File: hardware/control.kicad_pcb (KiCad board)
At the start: 2 copper layers, 49 parts, among them P1 POWER, P2 POWER, P3 DATA, P4 DATA, P5 ISP, P6 CONN_1, P7 CONN_1, P8 DISPLAY, P9 I2C, Q1 NX2301P, Q10 NX2301P, Q11 NX2301P, Q12 NX2301P, Q13 NX2301P, Q14 NX2301P, Q15 NX2301P, Q16 NX2301P, Q2 NX2301P, Q3 NX2301P, Q4 NX2301P, Q5 NX2301P, Q6 NX2301P, Q7 NX2301P, Q8 NX2301P, Q9 NX2301P, SW1 RESET, U1 AP1509, U2 ATMEGA328P-P, U3 74HC138, U4 74HC138, U5 TLC5940, X1 16MHz

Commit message: Final hardware tweaks.
Signed-off-by: Paul Brook <paul@nowt.org>
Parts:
- Q1, Q10, Q11, Q12, Q13, Q14, Q15, Q16, Q2, Q3, Q4, Q5, Q6, Q7, Q8, Q9: footprint SOT23GDS -> SOT23GDS_NP

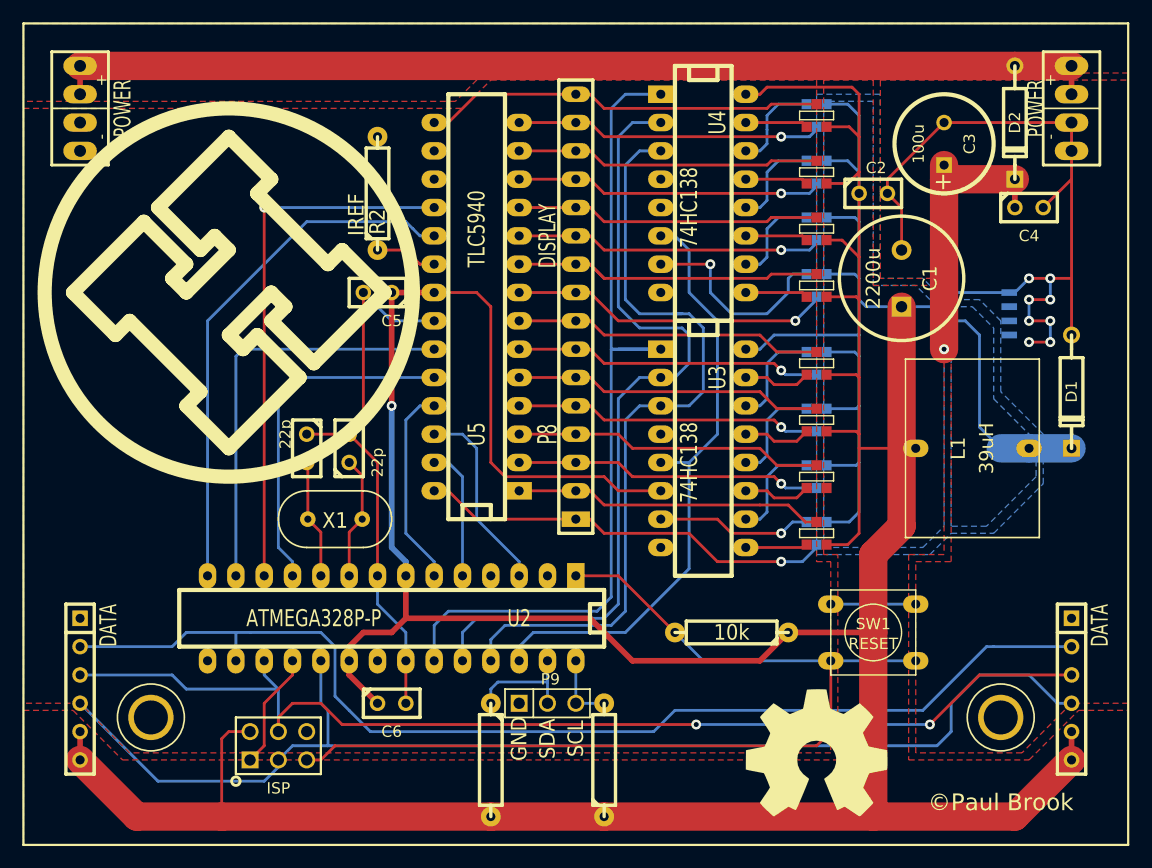
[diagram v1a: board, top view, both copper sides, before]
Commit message: PCB fixes.
Tweak power plane. Move mounting holes. Fix soldermask on power
connector.

Signed-off-by: Paul Brook <paul@nowt.org>
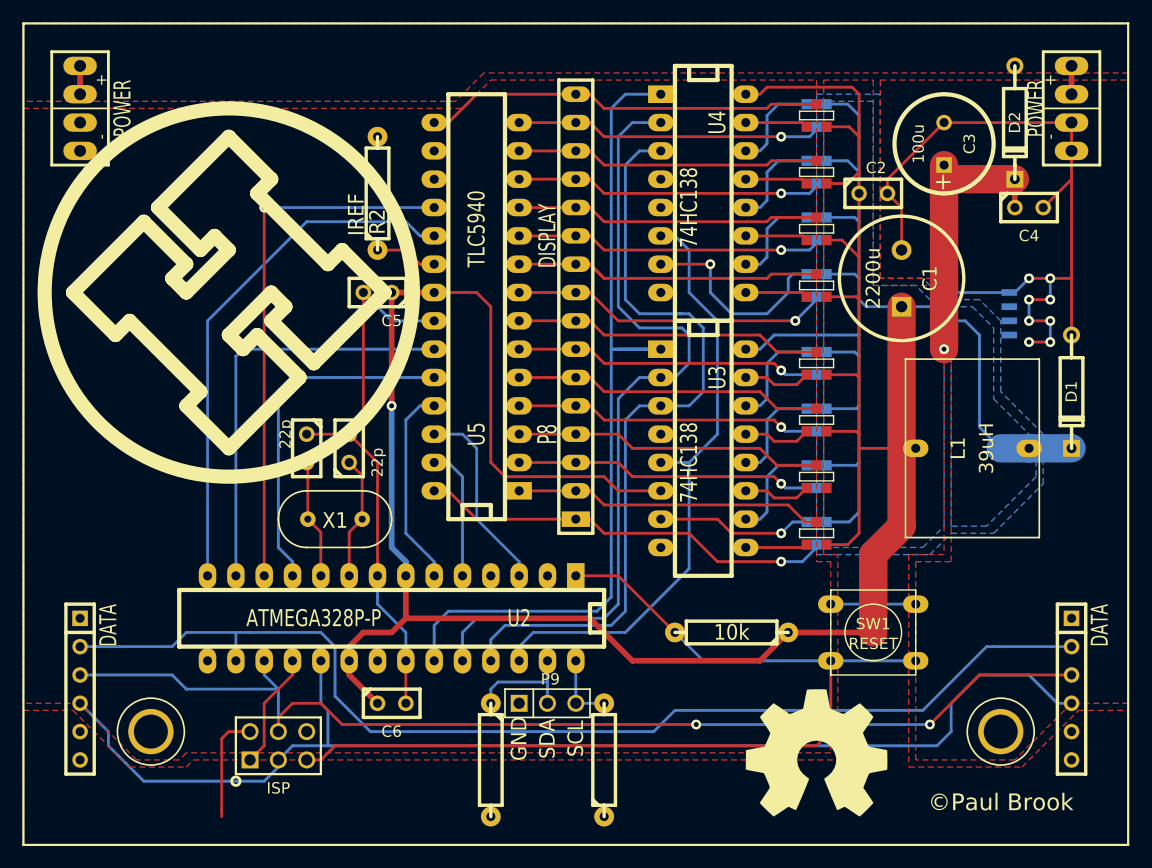
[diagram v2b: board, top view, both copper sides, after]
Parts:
- moved P6 1.27 mm to (139.7, 115.6)
- moved P7 1.27 mm to (63.5, 115.6)
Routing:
- net /5v: track 438.6 -> 323.9 mm
- net /raw: track 94.0 -> 5.08 mm
- net /SCK: track 106.5 -> 107.3 mm
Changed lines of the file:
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@@
-(kicad_pcb (version 3) (host pcbnew "(2013-dec-23)-stable")
+(kicad_pcb (version 3) (host pcbnew "(22-Jun-2014 BZR 4027)-stable")
   (general
     (links 163)
@@
     (thickness 1.6)
     (drawings 13)
-    (tracks 520)
+    (tracks 510)
     (zones 0)
     (modules 49)
@@
   (layers
     (15 F.Cu signal)
-    (0 B.Cu signal)
+    (0 B.Cu signal hide)
     (16 B.Adhes user)
     (17 F.Adhes user)
@@
     (mod_text_size 1 1)
     (mod_text_width 0.15)
-    (pad_size 2.286 1.5748)
-    (pad_drill 0.8128)
+    (pad_size 1.651 3.01498)
+    (pad_drill 1.0668)
     (pad_to_mask_clearance 0)
     (aux_axis_origin 0 0)
@@
   )
   (module HOLE3 (layer F.Cu)
-    (at 63.5 114.3)
+    (at 63.5 115.57)
     (fp_text reference P7 (at 0 0) (layer F.SilkS) hide
       (effects (font (size 1.524 1.524) (thickness 0.3048)))
@@
   )
   (module HOLE3 (layer F.Cu)
-    (at 139.7 114.3)
+    (at 139.7 115.57)
     (fp_text reference P6 (at 0 0) (layer F.SilkS) hide
       (effects (font (size 1.524 1.524) (thickness 0.3048)))
@@
     (fp_line (start 5.08 -2.54) (end 5.08 2.54) (layer F.SilkS) (width 0.254))
     (pad 1 thru_hole oval (at -1.27 0 90) (size 1.651 3.01498) (drill 1.0668)
-      (layers *.Cu F.Paste F.SilkS F.Mask)
+      (layers *.Cu *.Mask F.Paste F.SilkS)
       (net 23 /GND)
     )
     (pad 2 thru_hole oval (at 1.27 0 90) (size 1.651 3.01498) (drill 1.0668)
-      (layers *.Cu F.Paste F.SilkS F.Mask)
+      (layers *.Cu *.Mask F.Paste F.SilkS)
       (net 56 /raw)
     )
     (pad 1 thru_hole oval (at -3.81 0 90) (size 1.651 3.01498) (drill 1.0668)
-      (layers *.Cu F.Paste F.SilkS F.Mask)
+      (layers *.Cu *.Mask F.Paste F.SilkS)
       (net 23 /GND)
     )
     (pad 2 thru_hole oval (at 3.81 0 90) (size 1.651 3.01498) (drill 1.0668)
-      (layers *.Cu F.Paste F.SilkS F.Mask)
+      (layers *.Cu *.Mask F.Paste F.SilkS)
       (net 56 /raw)
     )
@@
     (fp_line (start 5.08 -2.54) (end 5.08 2.54) (layer F.SilkS) (width 0.254))
     (pad 1 thru_hole oval (at -1.27 0 90) (size 1.651 3.01498) (drill 1.0668)
-      (layers *.Cu F.Paste F.SilkS F.Mask)
+      (layers *.Cu *.Mask F.Paste F.SilkS)
       (net 23 /GND)
     )
     (pad 2 thru_hole oval (at 1.27 0 90) (size 1.651 3.01498) (drill 1.0668)
-      (layers *.Cu F.Paste F.SilkS F.Mask)
+      (layers *.Cu *.Mask F.Paste F.SilkS)
       (net 56 /raw)
     )
     (pad 1 thru_hole oval (at -3.81 0 90) (size 1.651 3.01498) (drill 1.0668)
-      (layers *.Cu F.Paste F.SilkS F.Mask)
+      (layers *.Cu *.Mask F.Paste F.SilkS)
       (net 23 /GND)
     )
     (pad 2 thru_hole oval (at 3.81 0 90) (size 1.651 3.01498) (drill 1.0668)
-      (layers *.Cu F.Paste F.SilkS F.Mask)
+      (layers *.Cu *.Mask F.Paste F.SilkS)
       (net 56 /raw)
     )
@@
   (segment (start 125.984 59.309) (end 124.079 59.309) (width 0.254) (layer B.Cu) (net 2))
   (segment (start 127 60.325) (end 125.984 59.309) (width 0.254) (layer B.Cu) (net 2))
-  (segment (start 146.05 115.57) (end 146.05 118.11) (width 0.508) (layer F.Cu) (net 2))
-  (segment (start 57.15 115.57) (end 57.15 118.11) (width 0.508) (layer F.Cu) (net 2))
   (segment (start 135.128 77.47) (end 130.81 77.47) (width 0.254) (layer B.Cu) (net 2))
   (segment (start 109.22 93.98) (end 105.41 93.98) (width 0.254) (layer F.Cu) (net 2))
@@
   (segment (start 118.11 109.22) (end 106.68 109.22) (width 0.508) (layer F.Cu) (net 2))
   (segment (start 120.65 106.68) (end 128.27 106.68) (width 0.508) (layer F.Cu) (net 2))
-  (segment (start 146.05 118.11) (end 140.97 123.19) (width 2.54) (layer F.Cu) (net 2))
-  (segment (start 62.23 123.19) (end 57.15 118.11) (width 2.54) (layer F.Cu) (net 2))
-  (segment (start 140.97 123.19) (end 128.27 123.19) (width 2.54) (layer F.Cu) (net 2))
-  (segment (start 128.27 123.19) (end 104.14 123.19) (width 2.54) (layer F.Cu) (net 2))
-  (segment (start 104.14 123.19) (end 93.98 123.19) (width 2.54) (layer F.Cu) (net 2))
-  (segment (start 93.98 123.19) (end 69.85 123.19) (width 2.54) (layer F.Cu) (net 2))
-  (segment (start 69.85 123.19) (end 62.23 123.19) (width 2.54) (layer F.Cu) (net 2))
   (segment (start 130.81 77.47) (end 130.81 97.155) (width 2.54) (layer F.Cu) (net 2))
   (segment (start 128.27 99.695) (end 128.27 106.68) (width 2.54) (layer F.Cu) (net 2))
-  (segment (start 128.27 106.68) (end 128.27 123.19) (width 2.54) (layer F.Cu) (net 2))
   (segment (start 130.81 97.155) (end 128.27 99.695) (width 2.54) (layer F.Cu) (net 2))
   (segment (start 124.079 91.694) (end 126.746 91.694) (width 0.254) (layer B.Cu) (net 2))
@@
   (segment (start 104.14 59.69) (end 102.87 58.42) (width 0.254) (layer F.Cu) (net 46))
   (segment (start 102.87 58.42) (end 101.6 58.42) (width 0.254) (layer F.Cu) (net 46))
+  (segment (start 59.69 115.57) (end 59.69 116.84) (width 0.254) (layer B.Cu) (net 47))
+  (segment (start 62.865 120.015) (end 73.66 120.015) (width 0.254) (layer B.Cu) (net 47))
+  (segment (start 59.69 116.84) (end 62.865 120.015) (width 0.254) (layer B.Cu) (net 47))
   (segment (start 137.795 110.49) (end 135.255 113.03) (width 0.254) (layer B.Cu) (net 47))
   (segment (start 135.255 113.03) (end 135.255 115.57) (width 0.254) (layer B.Cu) (net 47))
@@
   (segment (start 137.795 110.49) (end 142.24 110.49) (width 0.254) (layer B.Cu) (net 47))
   (segment (start 74.93 118.11) (end 74.93 118.745) (width 0.254) (layer B.Cu) (net 47))
-  (segment (start 64.135 120.015) (end 57.15 113.03) (width 0.254) (layer B.Cu) (net 47))
-  (segment (start 73.66 120.015) (end 64.135 120.015) (width 0.254) (layer B.Cu) (net 47))
+  (segment (start 59.69 115.57) (end 57.15 113.03) (width 0.254) (layer B.Cu) (net 47))
   (segment (start 74.93 118.745) (end 73.66 120.015) (width 0.254) (layer B.Cu) (net 47))
   (segment (start 78.74 109.22) (end 78.74 113.03) (width 0.254) (layer B.Cu) (net 47))
@@
   (segment (start 146.05 58.42) (end 146.05 55.88) (width 0.508) (layer F.Cu) (net 56))
   (segment (start 57.15 58.42) (end 57.15 55.88) (width 0.508) (layer F.Cu) (net 56))
-  (segment (start 140.97 55.88) (end 57.15 55.88) (width 2.54) (layer F.Cu) (net 56))
-  (segment (start 146.05 55.88) (end 140.97 55.88) (width 2.54) (layer F.Cu) (net 56))
   (segment (start 77.5716 96.52) (end 77.5716 91.5416) (width 0.254) (layer F.Cu) (net 57))
   (segment (start 77.5716 91.5416) (end 77.47 91.44) (width 0.254) (layer F.Cu) (net 57))
@@
     (polygon
       (pts
-        (xy 124.46 117.475) (xy 61.595 117.475) (xy 57.15 113.03) (xy 52.07 113.03) (xy 52.07 59.69)
-        (xy 91.44 59.69) (xy 93.98 57.15) (xy 123.19 57.15) (xy 123.19 100.33) (xy 124.46 100.33)
+        (xy 124.46 117.475) (xy 66.675 117.475) (xy 66.04 118.11) (xy 62.23 118.11) (xy 57.15 113.03)
+        (xy 52.07 113.03) (xy 52.07 59.69) (xy 91.44 59.69) (xy 93.98 57.15) (xy 123.19 57.15)
+        (xy 123.19 100.33) (xy 124.46 100.33)
       )
     )
@@
     (polygon
       (pts
-        (xy 151.13 125.73) (xy 52.07 125.73) (xy 52.07 113.665) (xy 56.515 113.665) (xy 60.96 118.11)
-        (xy 125.095 118.11) (xy 125.095 99.695) (xy 123.825 99.695) (xy 123.825 57.15) (xy 128.27 57.15)
-        (xy 128.27 75.565) (xy 134.62 75.565) (xy 134.62 99.695) (xy 131.445 99.695) (xy 131.445 118.11)
-        (xy 142.24 118.11) (xy 146.685 113.665) (xy 151.13 113.665) (xy 151.13 125.73)
+        (xy 151.13 125.73) (xy 52.07 125.73) (xy 52.07 113.665) (xy 56.515 113.665) (xy 61.595 118.745)
+        (xy 66.675 118.745) (xy 67.31 118.11) (xy 125.095 118.11) (xy 125.095 99.695) (xy 123.825 99.695)
+        (xy 123.825 57.15) (xy 128.27 57.15) (xy 128.27 75.565) (xy 134.62 75.565) (xy 134.62 99.695)
+        (xy 131.445 99.695) (xy 131.445 118.745) (xy 141.605 118.745) (xy 146.685 113.665) (xy 151.13 113.665)
       )
     )
@@
     (polygon
       (pts
-        (xy 151.13 113.03) (xy 146.05 113.03) (xy 141.605 117.475) (xy 132.08 117.475) (xy 132.08 100.33)
+        (xy 151.13 113.03) (xy 146.05 113.03) (xy 140.97 118.11) (xy 132.08 118.11) (xy 132.08 100.33)
         (xy 135.255 100.33) (xy 135.255 74.93) (xy 128.905 74.93) (xy 128.905 57.15) (xy 151.13 57.15)
       )

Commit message: SMD inductor
Signed-off-by: Paul Brook <paul@nowt.org>
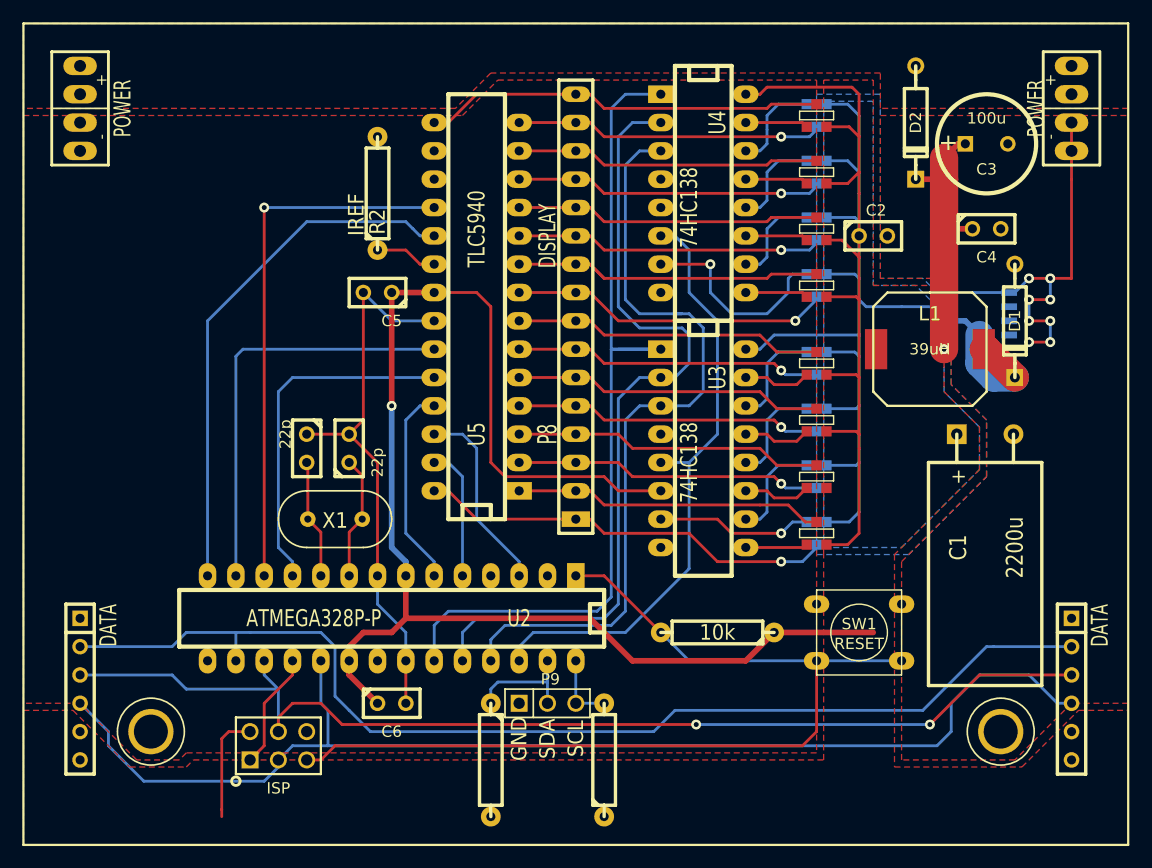
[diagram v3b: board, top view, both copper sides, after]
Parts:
- C1: footprint C2V10 -> CPR10X20
- G***, HACKSPACE_LOGO: moved to B.Cu
- L1: footprint INDUCTOR_TORROID -> self_cms_we-tpc_XL
- moved C1 15.9 mm to (138.4, 88.9)
- moved L1 9.67 mm to (133.3, 81.3), turned to 0 degrees
- moved D2 8.89 mm to (132.1, 61.0)
- moved D1 8.13 mm to (141.0, 78.7)
- moved HACKSPACE_LOGO 6.38 mm to (71.1, 82.5)
- moved C4 4.26 mm to (138.4, 70.5)
- moved C2 3.81 mm to (128.3, 71.1)
- moved C3 3.81 mm to (138.4, 62.9), turned to 0 degrees
- moved SW1 1.27 mm to (127.0, 106.7)
- moved R1 1.27 mm to (114.3, 106.7)
- moved G*** 0.64 mm to (123.2, 118.1)
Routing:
- net /GND: track 129.3 -> 87.5 mm
- net /5v: track 323.9 -> 288.6 mm
- net /out: track 20.5 -> 13.3 mm
- net /raw: track 5.08 -> 0.00 mm
- net /RESET: track 88.0 -> 85.5 mm
- net /12v: track 26.9 -> 26.1 mm
- removed copper zone on B.Cu, net /out
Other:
- board text added: "10lol control rev2"
